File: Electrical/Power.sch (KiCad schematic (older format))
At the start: 14 parts

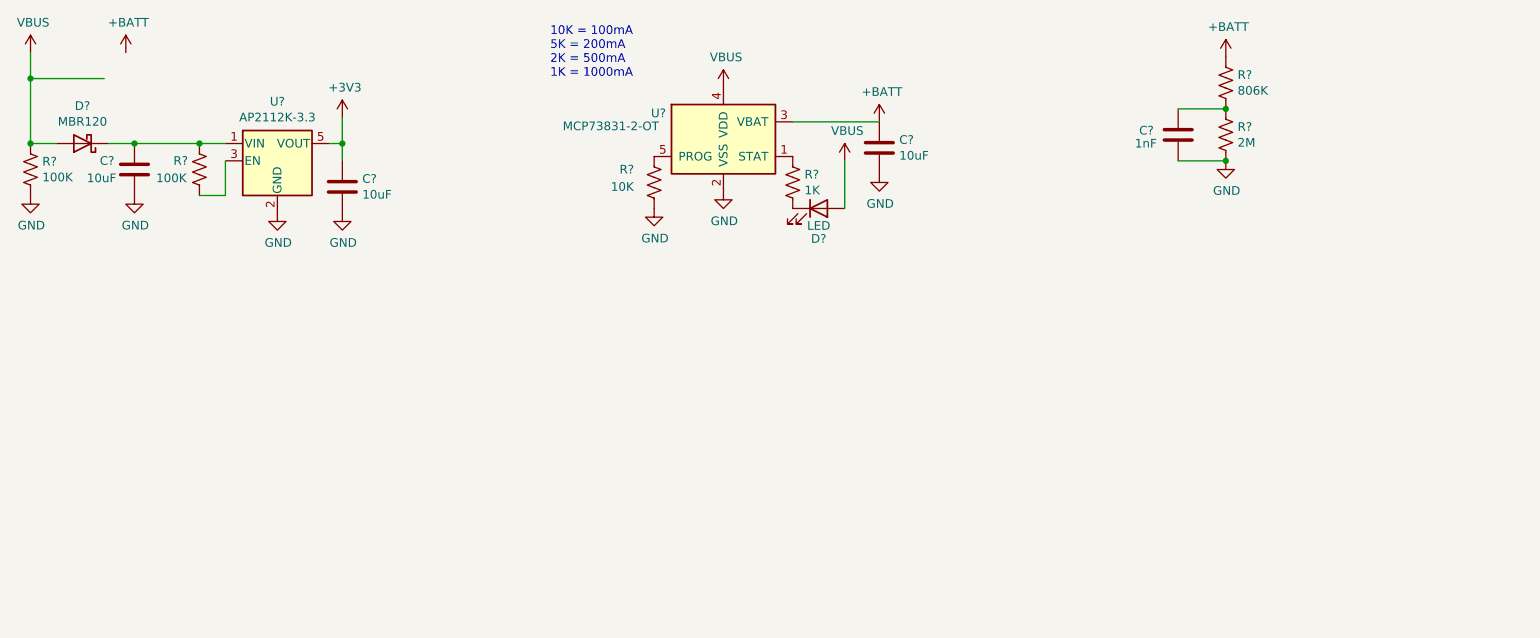
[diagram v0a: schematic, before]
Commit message: USB C and RGB IC Schematics
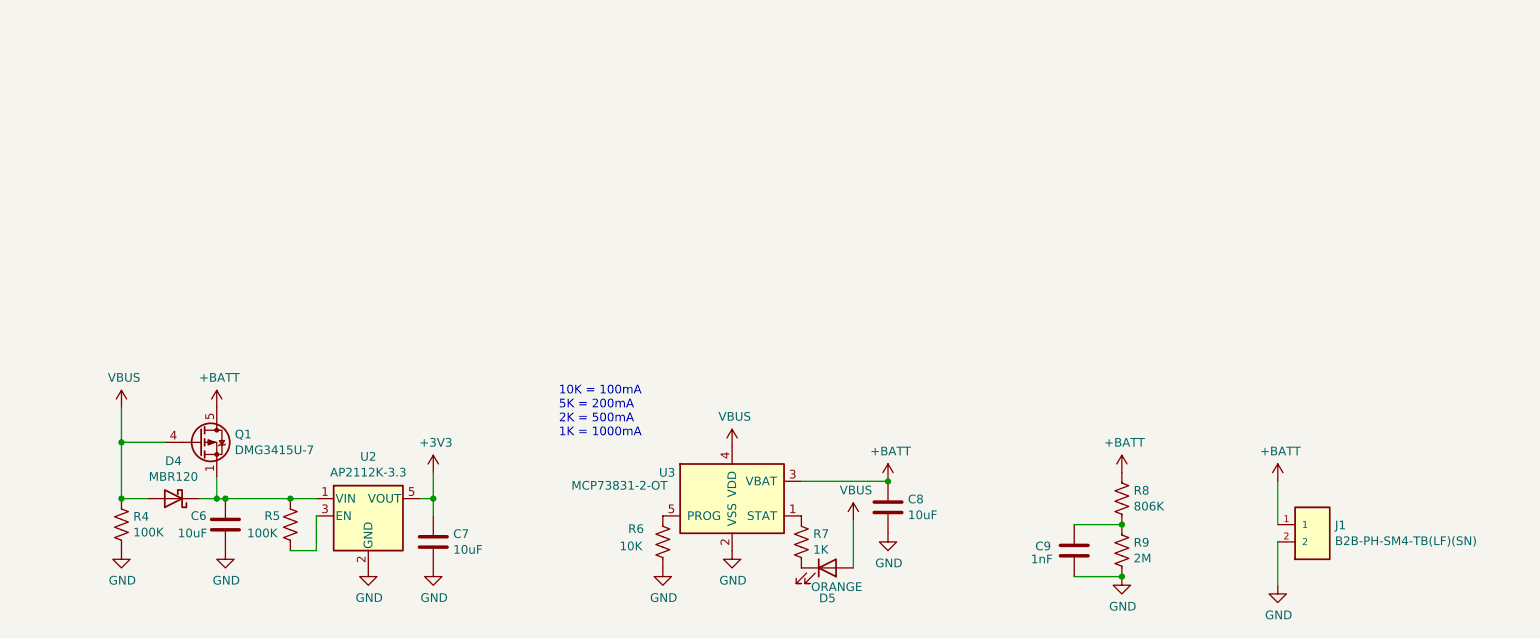
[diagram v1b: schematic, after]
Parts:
- added J1: B2B-PH-SM4-TB(LF)(SN), JST_B2B-PH-SM4-TB(LF)(SN), symbol B2B-PH-SM4-TB_LF__SN_:B2B-PH-SM4-TB(LF)(SN)
- added Q1: DMG3415U-7, DMG3415U-7:SOT95P240X105-3N, symbol Transistor_FET:DMP3013SFV
- D4: renamed from D?; footprint (none) -> MBR120:On_Semiconductor-MBR120VLSFT1-Manufacturer_Recommended
- D5: renamed from D?; value LED -> ORANGE
- gave numbers to parts that had none: 12
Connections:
- wire segments 16 -> 20
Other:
- moved on the sheet: C6, C7, C8, C9, D4, D5, R4, R5, R6, R7, R8, R9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
